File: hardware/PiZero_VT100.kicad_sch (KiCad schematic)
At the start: 41 parts, among them J1 GPIO, J2 RS232, J3 Ext. Power max,. 9V DC/AC, J4 Mini-DIN-6, J5 to Testpins 22(DM) and TP23(D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, J6 USB_A, J7 Z80-MBC2 direct, J8 LCD Power, J9 On / Off, K1 G5V-2, Q1 BC546, Q2 BC546, U1 LM350_TO220

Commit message: Additions to readme
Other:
- note added: "Imax = 40mA"
- note added: "Ion = 30mA"
- moved on the sheet: BZ1
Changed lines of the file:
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@@
 		(date "15 nov 2012")
 	)
+	(text "Imax = 40mA\n"
+		(exclude_from_sim no)
+		(at 124.968 112.014 0)
+		(effects
+			(font
+				(size 1.27 1.27)
+			)
+		)
+	)
 	(text "TxD\n"
 		(exclude_from_sim no)
@@
 		)
 	)
+	(text "Ion = 30mA"
+		(exclude_from_sim no)
+		(at 133.858 60.96 0)
+		(effects
+			(font
+				(size 1.27 1.27)
+			)
+		)
+	)
 	(text "MAX232 mit DB9 Stecker\nauf PCB"
 		(exclude_from_sim no)
@@
 	)
 	(junction
-		(at 109.22 116.84)
-		(diameter 0)
-		(color 0 0 0 0)
-	)
-	(junction
 		(at 95.25 173.99)
 		(diameter 0)
@@
 	)
 	(junction
-		(at 224.79 85.09)
+		(at 88.9 102.87)
 		(diameter 0)
 		(color 0 0 0 0)
 	)
 	(junction
-		(at 142.24 26.67)
+		(at 224.79 85.09)
 		(diameter 0)
 		(color 0 0 0 0)
 	)
 	(junction
-		(at 88.9 107.95)
+		(at 142.24 26.67)
 		(diameter 0)
 		(color 0 0 0 0)
@@
 	)
 	(junction
-		(at 109.22 100.33)
+		(at 109.22 102.87)
 		(diameter 0)
 		(color 0 0 0 0)
@@
 	)
 	(junction
+		(at 109.22 114.3)
+		(diameter 0)
+		(color 0 0 0 0)
+	)
+	(junction
 		(at 58.42 134.62)
 		(diameter 0)
@@
 	(wire
 		(pts
-			(xy 88.9 107.95) (xy 102.87 107.95)
+			(xy 88.9 102.87) (xy 109.22 102.87)
 		)
 		(stroke
@@
 	(wire
 		(pts
-			(xy 115.57 105.41) (xy 115.57 116.84)
+			(xy 115.57 107.95) (xy 115.57 114.3)
 		)
 		(stroke
@@
 	(wire
 		(pts
-			(xy 109.22 100.33) (xy 102.87 100.33)
-		)
-		(stroke
-			(width 0)
-			(type default)
-		)
-	)
-	(wire
-		(pts
 			(xy 60.96 30.48) (xy 31.75 30.48)
 		)
@@
 	(wire
 		(pts
-			(xy 73.66 107.95) (xy 88.9 107.95)
+			(xy 73.66 102.87) (xy 88.9 102.87)
 		)
 		(stroke
@@
 	(wire
 		(pts
-			(xy 109.22 100.33) (xy 109.22 105.41)
+			(xy 109.22 102.87) (xy 109.22 105.41)
 		)
 		(stroke
@@
 	(wire
 		(pts
-			(xy 109.22 116.84) (xy 102.87 116.84)
-		)
-		(stroke
-			(width 0)
-			(type default)
-		)
-	)
-	(wire
-		(pts
 			(xy 113.03 45.72) (xy 113.03 46.99)
 		)
@@
 	(wire
 		(pts
-			(xy 102.87 100.33) (xy 102.87 107.95)
-		)
-		(stroke
-			(width 0)
-			(type default)
-		)
-	)
-	(wire
-		(pts
 			(xy 142.24 26.67) (xy 142.24 31.75)
 		)
@@
 	(wire
 		(pts
-			(xy 96.52 114.3) (xy 102.87 114.3)
+			(xy 96.52 114.3) (xy 109.22 114.3)
 		)
 		(stroke
@@
 	(wire
 		(pts
-			(xy 102.87 116.84) (xy 102.87 114.3)
-		)
-		(stroke
-			(width 0)
-			(type default)
-		)
-	)
-	(wire
-		(pts
 			(xy 220.98 140.97) (xy 222.25 140.97)
 		)
@@
 	(wire
 		(pts
-			(xy 115.57 100.33) (xy 109.22 100.33)
+			(xy 115.57 102.87) (xy 109.22 102.87)
 		)
 		(stroke
@@
 	(wire
 		(pts
-			(xy 88.9 106.68) (xy 88.9 107.95)
-		)
-		(stroke
-			(width 0)
-			(type default)
-		)
-	)
-	(wire
-		(pts
 			(xy 208.28 90.17) (xy 224.79 90.17)
 		)
@@
 	(wire
 		(pts
-			(xy 73.66 111.76) (xy 73.66 107.95)
+			(xy 73.66 111.76) (xy 73.66 102.87)
 		)
 		(stroke
@@
 	(wire
 		(pts
-			(xy 115.57 116.84) (xy 109.22 116.84)
+			(xy 115.57 114.3) (xy 109.22 114.3)
+		)
+		(stroke
+			(width 0)
+			(type default)
+		)
+	)
+	(wire
+		(pts
+			(xy 88.9 102.87) (xy 88.9 101.6)
 		)
 		(stroke
@@
 	(wire
 		(pts
-			(xy 109.22 113.03) (xy 109.22 116.84)
+			(xy 109.22 113.03) (xy 109.22 114.3)
 		)
 		(stroke
@@
 	(symbol
 		(lib_id "power:+5V")
-		(at 88.9 106.68 0)
+		(at 88.9 101.6 0)
 		(unit 1)
 		(exclude_from_sim no)
@@
 		(dnp no)
 		(property "Reference" "#PWR019"
-			(at 88.9 110.49 0)
+			(at 88.9 105.41 0)
 			(effects
 				(font
@@
 		)
 		(property "Value" "+5V"
-			(at 89.2683 102.3556 0)
+			(at 89.2683 97.2756 0)
 			(effects
 				(font
@@
 		)
 		(property "Footprint" ""
-			(at 88.9 106.68 0)
+			(at 88.9 101.6 0)
 			(effects
 				(font
@@
 		)
 		(property "Datasheet" ""
-			(at 88.9 106.68 0)
+			(at 88.9 101.6 0)
 			(effects
 				(font
@@
 		)
 		(property "Description" "Power symbol creates a global label with name \"+5V\""
-			(at 88.9 106.68 0)
+			(at 88.9 101.6 0)
 			(effects
 				(font
@@
 	(symbol
 		(lib_id "Device:Buzzer")
-		(at 118.11 102.87 0)
+		(at 118.11 105.41 0)
 		(unit 1)
 		(exclude_from_sim no)
@@
 		(fields_autoplaced yes)
 		(property "Reference" "BZ1"
-			(at 121.92 101.5999 0)
+			(at 121.92 104.1399 0)
 			(effects
 				(font
@@
 		)
 		(property "Value" "Buzzer"
-			(at 121.92 104.1399 0)
+			(at 121.92 106.6799 0)
 			(effects
 				(font
@@
 		)
 		(property "Footprint" "Buzzer_Beeper:Buzzer_TDK_PS1240P02BT_D12.2mm_H6.5mm"
-			(at 117.475 100.33 90)
+			(at 117.475 102.87 90)
 			(effects
 				(font
@@
 		)
 		(property "Datasheet" "~"
-			(at 117.475 100.33 90)
+			(at 117.475 102.87 90)
 			(effects
 				(font
@@
 		)
 		(property "Description" "Buzzer, polarized"
-			(at 118.11 102.87 0)
+			(at 118.11 105.41 0)
 			(effects
 				(font
@@
 		(on_board yes)
 		(dnp no)
-		(fields_autoplaced yes)
 		(property "Reference" "D5"
 			(at 111.76 107.9499 90)
@@
 		)
 		(property "Value" "1N4148"
-			(at 111.76 110.4899 90)
+			(at 101.346 112.268 90)
 			(effects
 				(font

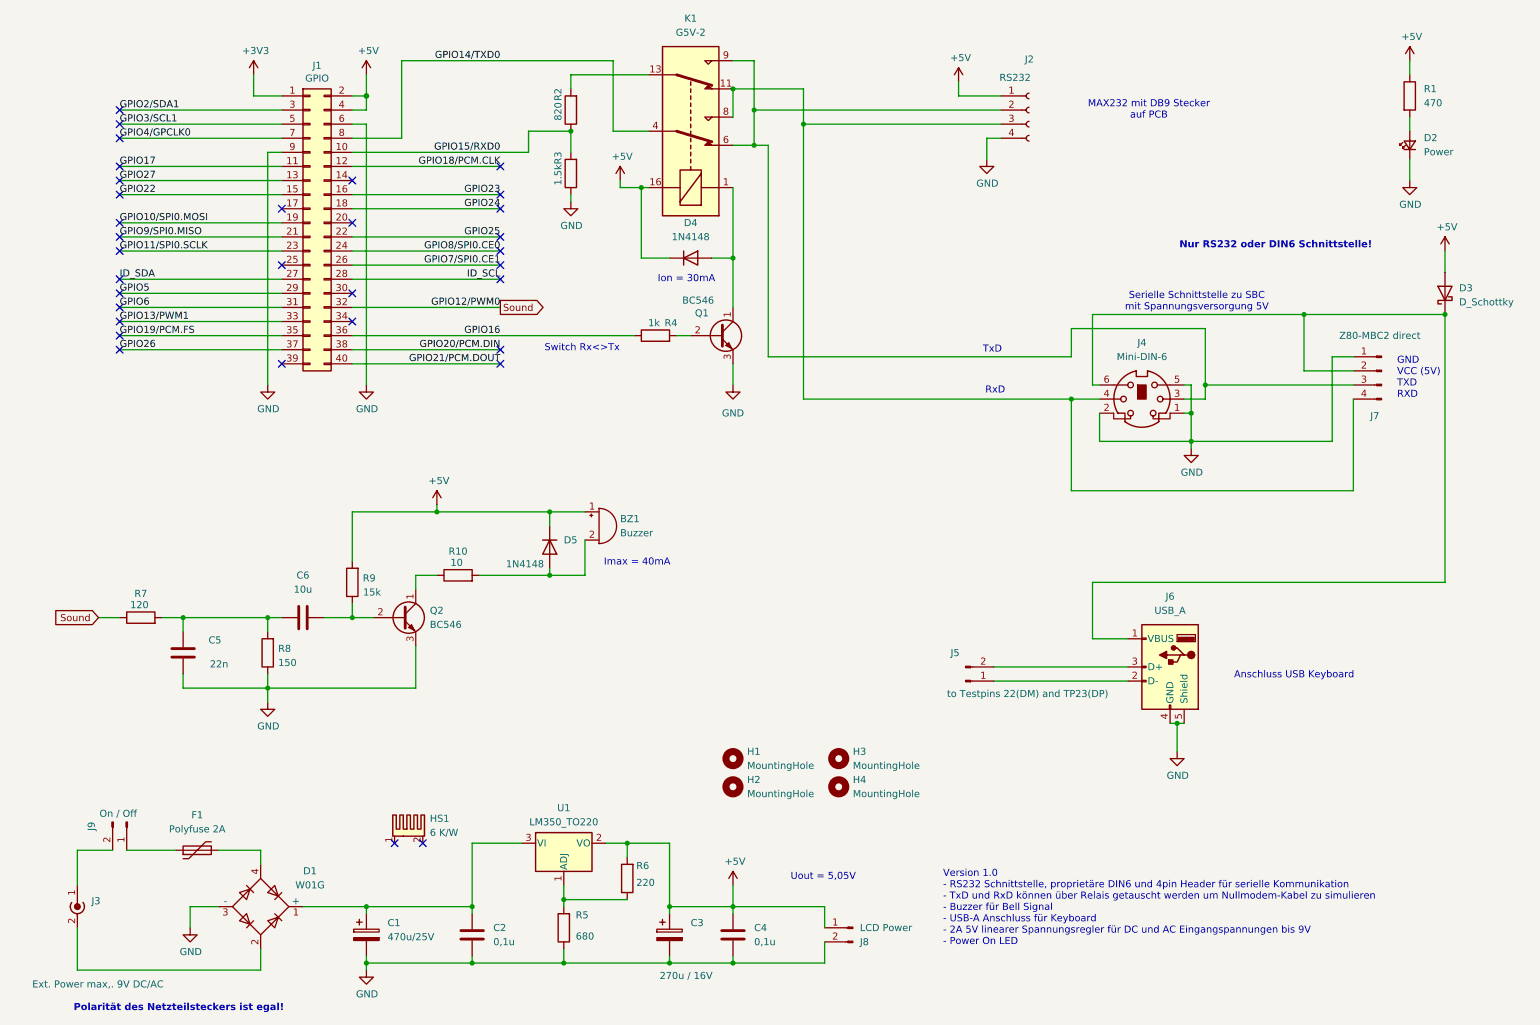
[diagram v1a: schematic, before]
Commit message: Adapterplatine V2.0 mit Schaltregler. da Linearregler zu hohe Wärmeentwicklung hat
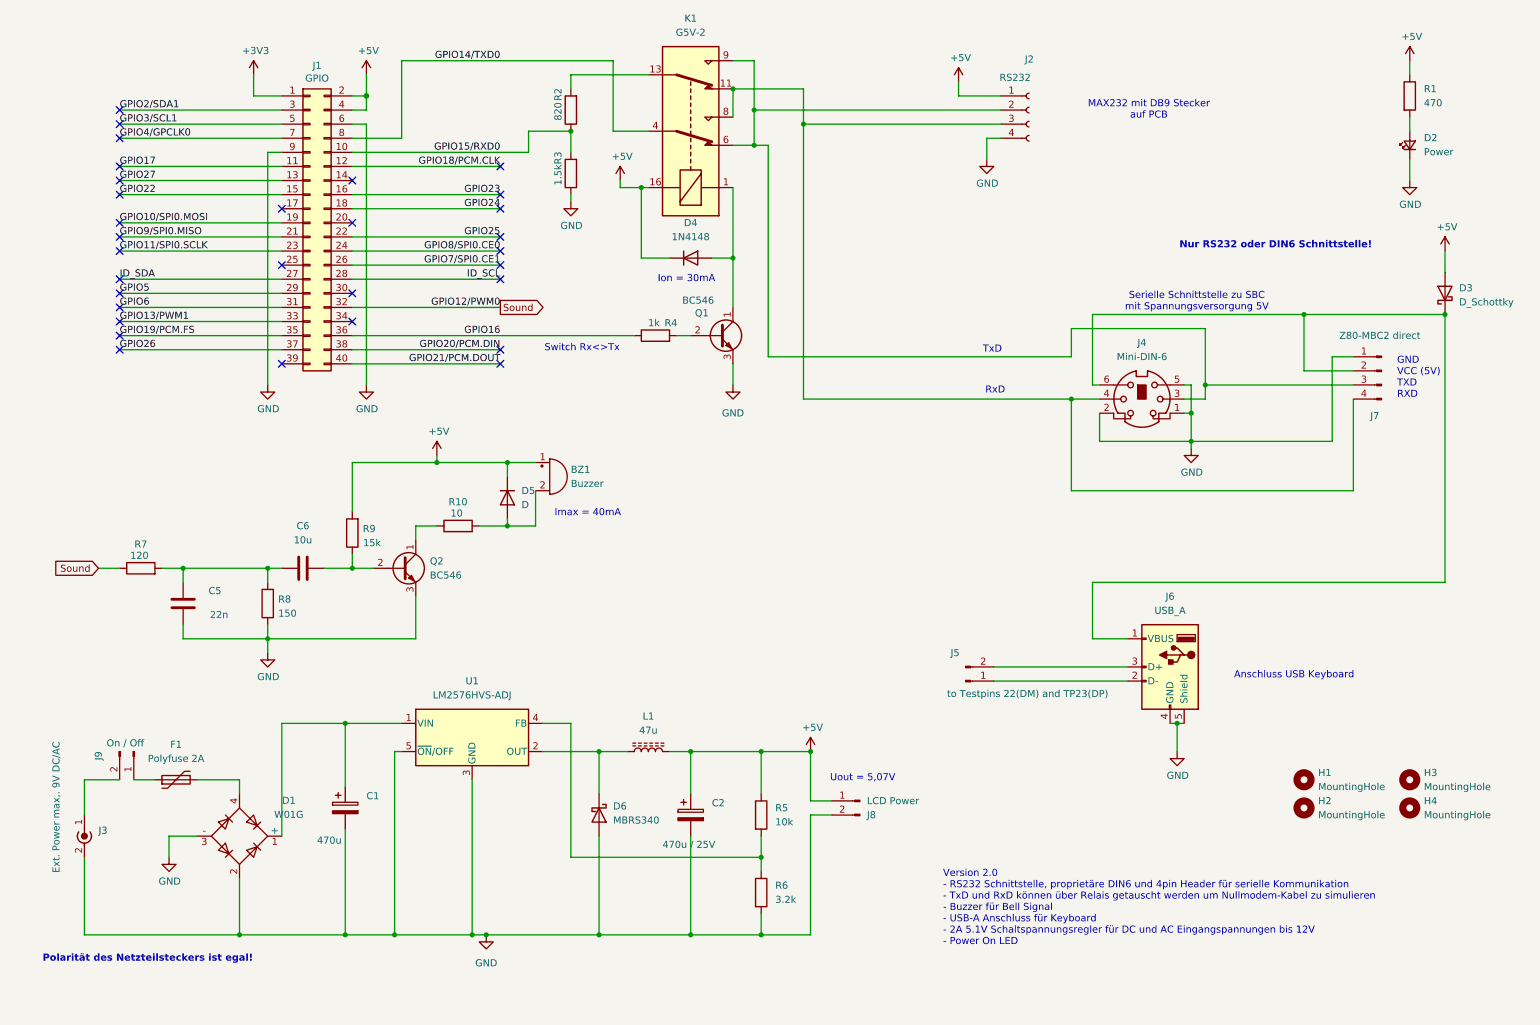
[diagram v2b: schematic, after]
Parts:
- removed C2, C4: 0,1u, Capacitor_THT:C_Disc_D5.0mm_W2.5mm_P5.00mm, symbol Device:C
- removed C3: 270u / 16V, Capacitor_THT:CP_Radial_D10.0mm_P5.00mm, symbol Device:C_Polarized
- removed HS1: 6 K/W, Heatsink:Heatsink_Fischer_SK104-STCB_35x13mm__2xDrill3.5mm_ScrewM3, symbol Mechanical:Heatsink_Pad_2Pin
- removed U1: LM350_TO220, Package_TO_SOT_THT:TO-220-3_Vertical, symbol Regulator_Linear:LM350_TO220
- added C2: 470u / 25V, Capacitor_SMD:CP_Elec_10x10, symbol Device:C_Polarized
- added D6: MBRS340, Diode_SMD:D_SMC, symbol Diode:MBRS340
- added L1: 47u, Inductor_SMD:L_Fastron_PISN, symbol Device:L_Ferrite
- added U1: LM2576HVS-ADJ, Package_TO_SOT_SMD:TO-263-5_TabPin3, symbol Regulator_Switching:LM2576HVS-ADJ
- BZ1: footprint Buzzer_Beeper:Buzzer_TDK_PS1240P02BT_D12.2mm_H6.5mm -> Buzzer_Beeper:MagneticBuzzer_ProSignal_ABI-009-RC
- C1: value 470u/25V -> 470u; footprint Capacitor_THT:CP_Radial_D10.0mm_P5.00mm -> Capacitor_SMD:CP_Elec_10x10
- D5: value 1N4148 -> D; footprint Diode_THT:D_A-405_P12.70mm_Horizontal -> Diode_THT:D_5W_P10.16mm_Horizontal
- R5: value 680 -> 10k; footprint Resistor_THT:R_Axial_DIN0207_L6.3mm_D2.5mm_P10.16mm_Horizontal -> Resistor_SMD:R_1206_3216Metric_Pad1.30x1.75mm_HandSolder
- R6: value 220 -> 3.2k; footprint Resistor_THT:R_Axial_DIN0207_L6.3mm_D2.5mm_P10.16mm_Horizontal -> Resistor_SMD:R_1206_3216Metric_Pad1.30x1.75mm_HandSolder
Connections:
- net +5V: now also R5.1, C2.1, L1.2; no longer R6.2
- net GND: now also D1.2, J3.2 (Ext), R6.2, C2.2, D6.2 (A), U1.3 (GND), U1.5 (~{ON}/OFF); no longer R5.1
- net at R5.2, R6.1: now also U1.4 (FB)
- net at C1.1, D1.1 (+): now also U1.1 (VIN)
- new net: D6.1 (K), L1.1, U1.2 (OUT)
- no-connect marks 33 -> 31
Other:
- note added: "Uout = 5,07V"
- note added: "Version 2.0 - RS232 Schnittstelle, proprietäre DIN6 und 4pin Header für serielle Kommunikation - TxD und RxD können über Relais getauscht werden um Nullmodem-Kabel zu simulieren - Buzzer für Bell Signal - USB-A Anschluss für Keyboard - 2A 5.1V Schaltspannungsregler für DC und AC Eingangspannungen bis 12V - Power On LED"
- note removed: "Uout = 5,05V"
- note removed: "Version 1.0 - RS232 Schnittstelle, proprietäre DIN6 und 4pin Header für serielle Kommunikation - TxD und RxD können über Relais getauscht werden um Nullmodem-Kabel zu simulieren - Buzzer für Bell Signal - USB-A Anschluss für Keyboard - 2A 5V linearer Spannungsregler für DC und AC Eingangspannungen bis 9V - Power On LED"
- moved on the sheet: BZ1, C5, C6, D1, F1, H1, H2, H3, H4, J3, J8, J9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

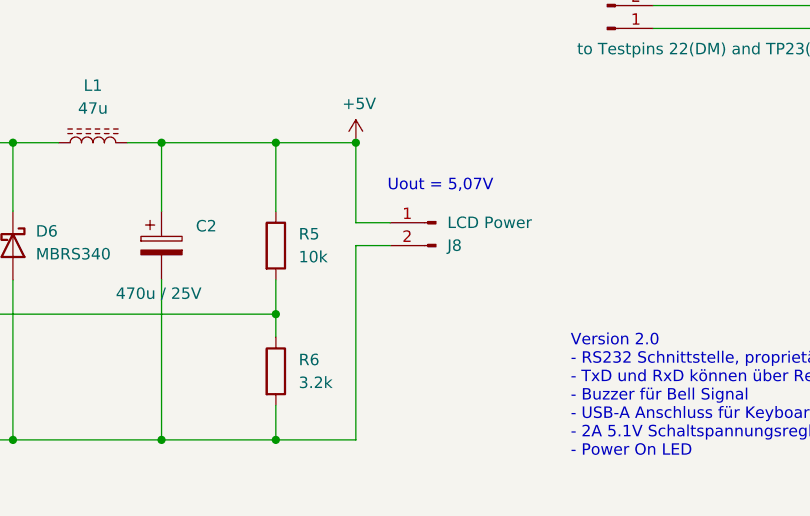
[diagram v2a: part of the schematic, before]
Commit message: Änderungen in Schematic
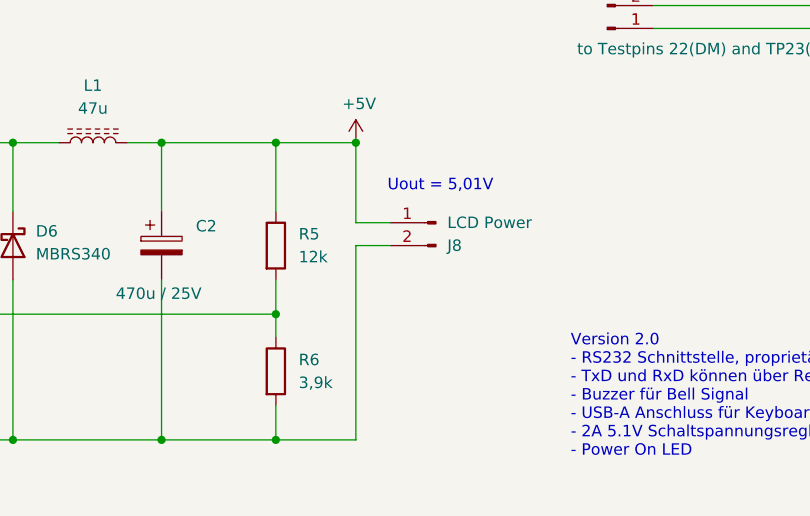
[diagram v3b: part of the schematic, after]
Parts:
- R5: value 10k -> 12k
- R6: value 3.2k -> 3,9k
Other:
- note added: "Uout = 5,01V"
- note removed: "Uout = 5,07V"
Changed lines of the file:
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@@
 		)
 	)
-	(text "Uout = 5,07V\n"
+	(text "Uout = 5,01V\n"
 		(exclude_from_sim no)
 		(at 165.608 150.876 0)
@@
 			)
 		)
-		(property "Value" "10k"
+		(property "Value" "12k"
 			(at 149.86 158.7499 0)
 			(effects
@@
 			)
 		)
-		(property "Value" "3.2k"
+		(property "Value" "3,9k"
 			(at 149.86 172.7199 0)
 			(effects

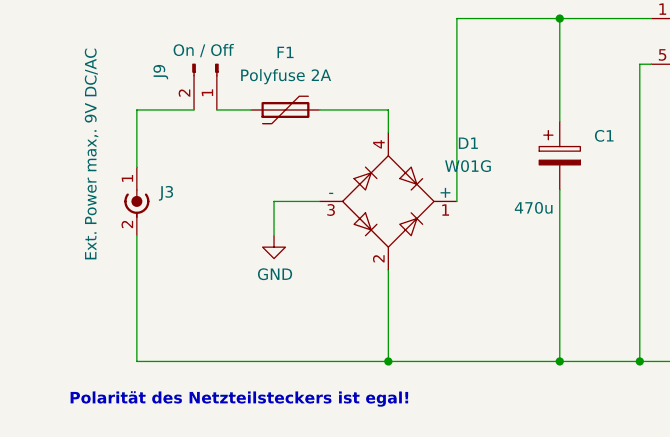
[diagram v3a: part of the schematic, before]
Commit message: PCB Adapterboard geändert
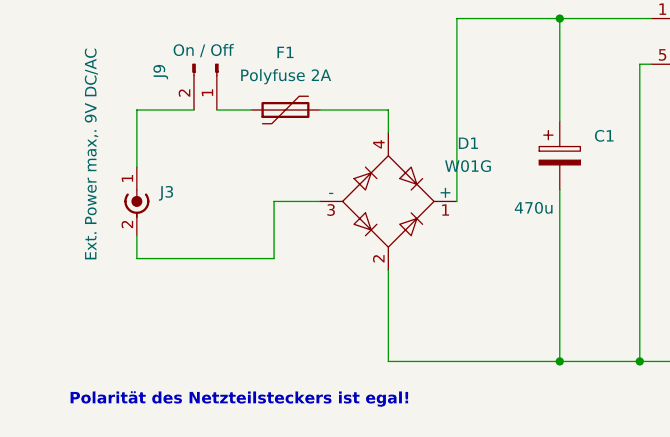
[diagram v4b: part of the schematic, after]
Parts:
- D4: footprint Diode_THT:D_A-405_P12.70mm_Horizontal -> Diode_THT:D_A-405_P10.16mm_Horizontal
- D5: footprint Diode_THT:D_5W_P10.16mm_Horizontal -> Diode_THT:D_A-405_P10.16mm_Horizontal
- F1: footprint Fuse:Fuse_Littelfuse-LVR125 -> Fuse:Fuse_Littelfuse-LVR200
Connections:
- net GND: no longer D1.3 (-), J3.2 (Ext)
- new net: D1.3 (-), J3.2 (Ext)
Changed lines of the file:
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@@
 	)
 	(junction
-		(at 53.34 179.07)
-		(diameter 0)
-		(color 0 0 0 0)
-	)
-	(junction
 		(at 203.2 82.55)
 		(diameter 0)
@@
 	(wire
 		(pts
-			(xy 40.64 165.1) (xy 40.64 161.29)
+			(xy 40.64 161.29) (xy 40.64 167.64)
 		)
 		(stroke
@@
 	(wire
 		(pts
+			(xy 40.64 167.64) (xy 25.4 167.64)
+		)
+		(stroke
+			(width 0)
+			(type default)
+		)
+	)
+	(wire
+		(pts
 			(xy 160.02 157.48) (xy 156.21 157.48)
 		)
@@
 	(wire
 		(pts
-			(xy 25.4 179.07) (xy 53.34 179.07)
-		)
-		(stroke
-			(width 0)
-			(type default)
-		)
-	)
-	(wire
-		(pts
 			(xy 106.68 99.06) (xy 106.68 105.41)
 		)
@@
 	(wire
 		(pts
-			(xy 25.4 165.1) (xy 25.4 179.07)
+			(xy 25.4 165.1) (xy 25.4 167.64)
 		)
 		(stroke
@@
 	)
 	(symbol
-		(lib_id "power:GND")
-		(at 40.64 165.1 0)
-		(unit 1)
-		(exclude_from_sim no)
-		(in_bom yes)
-		(on_board yes)
-		(dnp no)
-		(property "Reference" "#PWR011"
-			(at 40.64 171.45 0)
-			(effects
-				(font
-					(size 1.27 1.27)
-				)
-				(hide yes)
-			)
-		)
-		(property "Value" "GND"
-			(at 40.7543 169.4244 0)
-			(effects
-				(font
-					(size 1.27 1.27)
-				)
-			)
-		)
-		(property "Footprint" ""
-			(at 40.64 165.1 0)
-			(effects
-				(font
-					(size 1.27 1.27)
-				)
-			)
-		)
-		(property "Datasheet" ""
-			(at 40.64 165.1 0)
-			(effects
-				(font
-					(size 1.27 1.27)
-				)
-			)
-		)
-		(property "Description" "Power symbol creates a global label with name \"GND\" , ground"
-			(at 40.64 165.1 0)
-			(effects
-				(font
-					(size 1.27 1.27)
-				)
-				(hide yes)
-			)
-		)
-		(pin "1"
-		)
-		(instances
-			(project "PiZero_VT100"
-				(path "/e63e39d7-6ac0-4ffd-8aa3-1841a4541b55"
-					(reference "#PWR011")
-					(unit 1)
-				)
-			)
-		)
-	)
-	(symbol
 		(lib_id "Device:R")
 		(at 73.66 106.68 180)
@@
 			)
 		)
-		(property "Footprint" "Diode_THT:D_5W_P10.16mm_Horizontal"
+		(property "Footprint" "Diode_THT:D_A-405_P10.16mm_Horizontal"
 			(at 101.6 100.33 0)
 			(effects
@@
 			)
 		)
-		(property "Footprint" "Fuse:Fuse_Littelfuse-LVR125"
+		(property "Footprint" "Fuse:Fuse_Littelfuse-LVR200"
 			(at 46.99 149.86 0)
 			(effects
@@
 			)
 		)
-		(property "Footprint" "Diode_THT:D_A-405_P12.70mm_Horizontal"
+		(property "Footprint" "Diode_THT:D_A-405_P10.16mm_Horizontal"
 			(at 134.62 57.15 0)
 			(effects

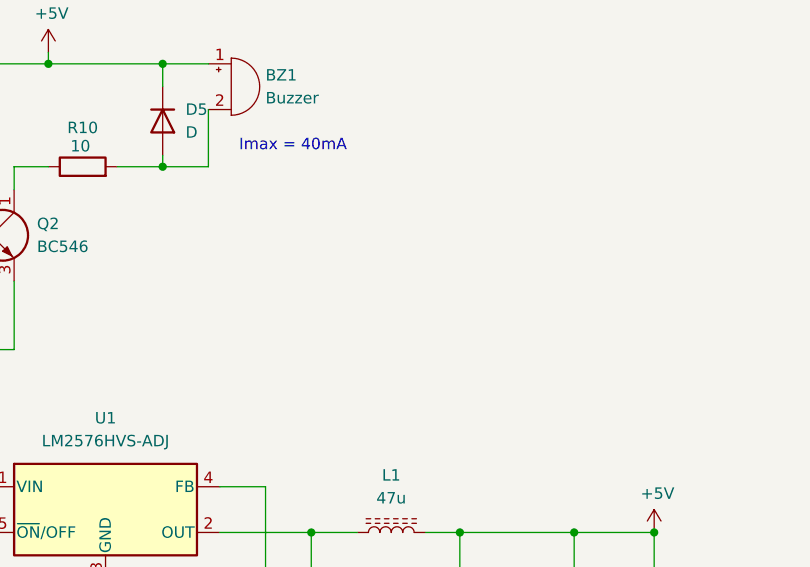
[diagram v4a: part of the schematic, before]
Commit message: Anmerkung zur Schaltung
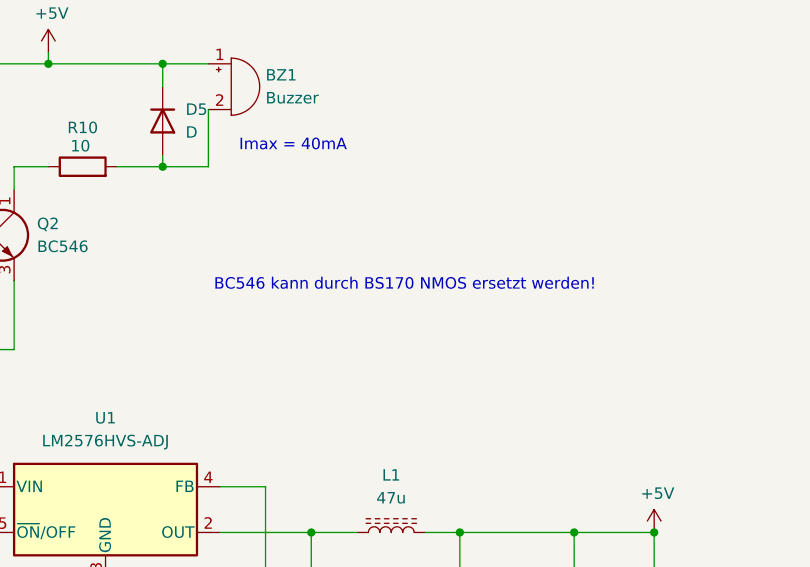
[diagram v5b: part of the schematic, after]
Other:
- note added: "BC546 kann durch BS170 NMOS ersetzt werden!"
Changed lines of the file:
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@@
+		)
+	)
+	(text "BC546 kann durch BS170 NMOS ersetzt werden!"
+		(exclude_from_sim no)
+		(at 128.524 118.618 0)
+		(effects
+			(font
+				(size 1.27 1.27)
+			)
 		)
 	)
